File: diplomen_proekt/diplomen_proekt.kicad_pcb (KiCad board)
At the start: 2 copper layers, 80.1 x 96 mm, 26 parts, among them SW1 SW_Push, U1 DA56-11SURKWA, U2 ESP32-S3, U3 HC-SR04, U4 ACTIVE_BUZZER, U5 TP4056, U6 MCP1826S

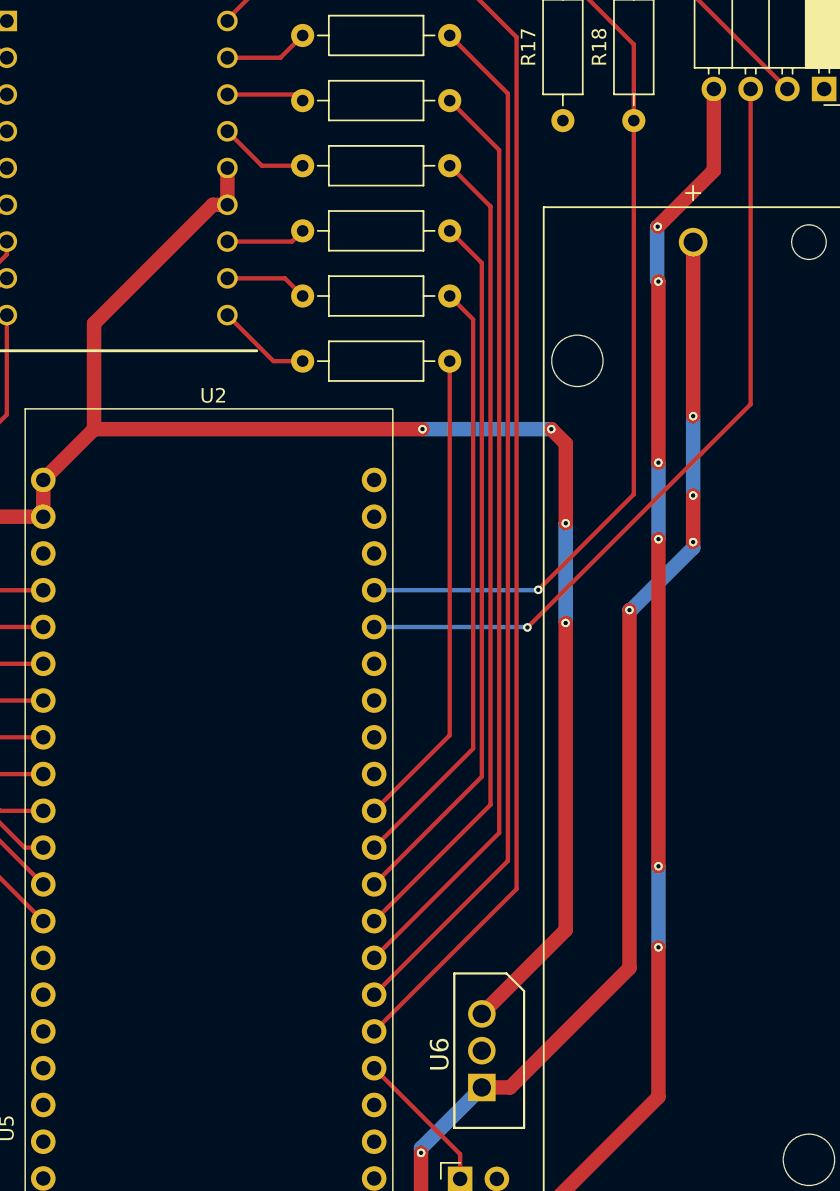
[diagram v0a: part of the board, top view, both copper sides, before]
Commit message: Small changes on the tracks
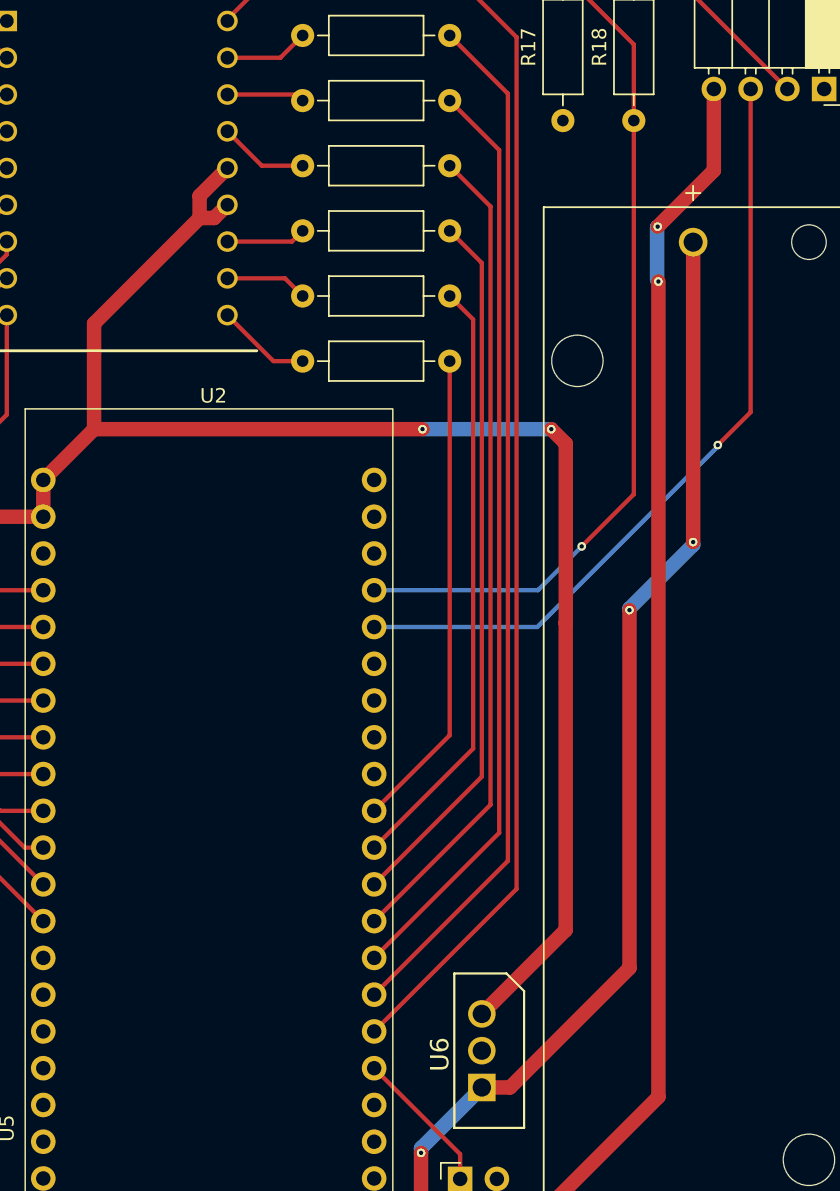
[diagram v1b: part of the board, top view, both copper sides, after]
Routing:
- net +3.3V: track 132.2 -> 133.9 mm, vias 6 -> 4
- net +5V: track 122.6 -> 122.4 mm, vias 8 -> 4
- net BAT: track 135.8 -> 135.7 mm, vias 5 -> 3
